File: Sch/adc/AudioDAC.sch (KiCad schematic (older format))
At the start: 22 parts, among them CN3 AudioJack, U6 NAU8822LYG

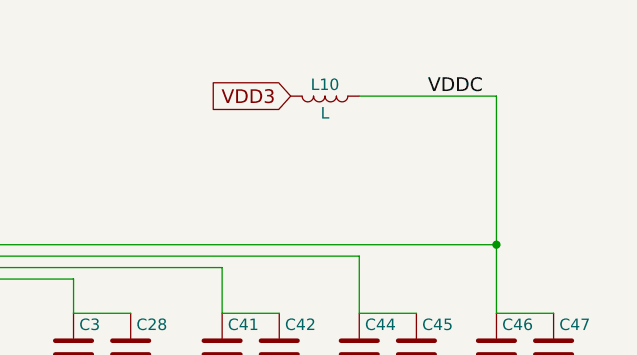
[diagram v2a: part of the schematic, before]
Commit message: Add 2 test headers
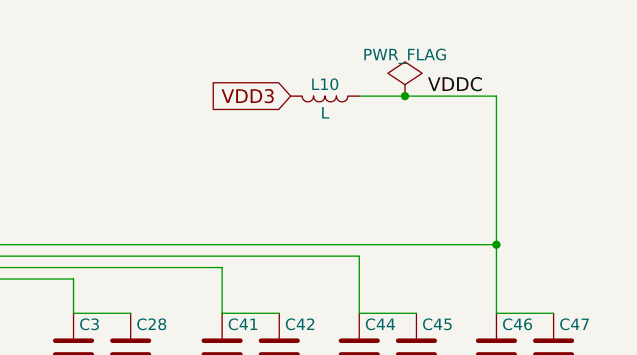
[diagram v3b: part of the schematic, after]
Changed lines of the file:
@@
 $EndComp
 $Comp
-L GND #PWR049
+L GND #PWR051
 U 1 1 58A94BF7
 P 7300 4600
-F 0 "#PWR049" H 7300 4350 50  0001 C CNN
+F 0 "#PWR051" H 7300 4350 50  0001 C CNN
 F 1 "GND" H 7300 4450 50  0000 C CNN
 F 2 "" H 7300 4600 50  0000 C CNN
@@
 $EndComp
 $Comp
-L GND #PWR050
+L GND #PWR052
 U 1 1 58A96033
 P 5650 5100
-F 0 "#PWR050" H 5650 4850 50  0001 C CNN
+F 0 "#PWR052" H 5650 4850 50  0001 C CNN
 F 1 "GND" H 5650 4950 50  0000 C CNN
 F 2 "" H 5650 5100 50  0000 C CNN
@@
 $EndComp
 $Comp
-L GND #PWR051
+L GND #PWR053
 U 1 1 58A98E4C
 P 7050 2800
-F 0 "#PWR051" H 7050 2550 50  0001 C CNN
+F 0 "#PWR053" H 7050 2550 50  0001 C CNN
 F 1 "GND" H 7050 2650 50  0000 C CNN
 F 2 "" H 7050 2800 50  0000 C CNN
@@
 $EndComp
 $Comp
-L GND #PWR052
+L GND #PWR054
 U 1 1 58A99758
 P 7700 2800
-F 0 "#PWR052" H 7700 2550 50  0001 C CNN
+F 0 "#PWR054" H 7700 2550 50  0001 C CNN
 F 1 "GND" H 7700 2650 50  0000 C CNN
 F 2 "" H 7700 2800 50  0000 C CNN
@@
 $EndComp
 $Comp
-L GND #PWR053
+L GND #PWR055
 U 1 1 58A997A8
 P 8300 2800
-F 0 "#PWR053" H 8300 2550 50  0001 C CNN
+F 0 "#PWR055" H 8300 2550 50  0001 C CNN
 F 1 "GND" H 8300 2650 50  0000 C CNN
 F 2 "" H 8300 2800 50  0000 C CNN
@@
 $EndComp
 $Comp
-L GND #PWR054
+L GND #PWR056
 U 1 1 58A99804
 P 8900 2800
-F 0 "#PWR054" H 8900 2550 50  0001 C CNN
+F 0 "#PWR056" H 8900 2550 50  0001 C CNN
 F 1 "GND" H 8900 2650 50  0000 C CNN
 F 2 "" H 8900 2800 50  0000 C CNN
@@
 100mW
 $Comp
-L +3V3 #PWR055
+L +3V3 #PWR057
 U 1 1 58B42B1D
 P 4750 1400
-F 0 "#PWR055" H 4750 1250 50  0001 C CNN
+F 0 "#PWR057" H 4750 1250 50  0001 C CNN
 F 1 "+3V3" H 4750 1540 50  0000 C CNN
 F 2 "" H 4750 1400 50  0000 C CNN
@@
 Text GLabel 7750 1550 0    60   Input ~ 0
 VDD3
+$Comp
+L PWR_FLAG #FLG058
+U 1 1 5992EBE5
+P 8250 1550
+F 0 "#FLG058" H 8250 1645 50  0001 C CNN
+F 1 "PWR_FLAG" H 8250 1730 50  0000 C CNN
+F 2 "" H 8250 1550 50  0000 C CNN
+F 3 "" H 8250 1550 50  0000 C CNN
+	1    8250 1550
+	1    0    0    -1
+$EndComp
+Connection ~ 8250 1550
 $EndSCHEMATC
